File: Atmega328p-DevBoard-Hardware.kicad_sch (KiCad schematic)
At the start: 28 parts, among them J1 Barrel_Jack, J2 DBG/PROG, J3 MTR1-CON, J4 MTR2-CON, SW1 SW_SPST, U1 L7805, U2 ATmega328P-A, U3 L293D, Y1 LFXTAL003237-Crystal-16MHz

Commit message: completed ssd section
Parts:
- added C16: 10uf, Capacitor_SMD:C_0805_2012Metric_Pad1.18x1.45mm_HandSolder, symbol Device:C_Small
- added C17: 0.1uf, Capacitor_SMD:C_0805_2012Metric_Pad1.18x1.45mm_HandSolder, symbol Device:C_Small
- added R10, R11, R12, R13, R14, R15: 1K, Resistor_SMD:R_0805_2012Metric_Pad1.20x1.40mm_HandSolder, symbol Device:R_Small_US
- added R3, R4, R5, R6, R7, R8, R9: 330R, Resistor_SMD:R_0805_2012Metric_Pad1.20x1.40mm_HandSolder, symbol Device:R_Small_US
- added U4: CD4511BE, Package_DIP:DIP-16_W7.62mm_LongPads, symbol 4xxx_IEEE:4511
- added U5: SC39-11YWA, Display_7Segment:Sx39-1xxxxx, symbol Display_Character:SC39-11YWA
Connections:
- net +5V: now also C16.1, C17.1, U4.16 (Vdd)
- net GND: now also C16.2, C17.2, R10.1, R11.1, R12.1, R13.1, R14.1, R15.1, U4.5 (~{EL}), U4.8 (Vss), U5.3 (CC), U5.8 (CC)
- new net: R5.1, U4.11 (Qc)
- new net: R5.2, U5.7 (C)
- new net: R7.1, U4.9 (Qe)
- new net: R7.2, U5.4 (E)
- new net: R3.1, U4.13 (Qa)
- new net: R3.2, U5.10 (A)
- new net: R6.1, U4.10 (Qd)
- new net: R6.2, U5.5 (D)
- new net: R8.1, U4.15 (Qf)
- new net: R8.2, U5.2 (F)
- new net: R4.1, U4.12 (Qb)
- new net: R4.2, U5.9 (B)
- new net: R9.1, U4.14 (Qg)
- new net: R9.2, U5.1 (G)
- new net BLANKING_INPUT_BL: R15.2, U4.4 (~{BI})
- new net LAMP_TEST_LT: R14.2, U4.3 (~{LT})
- new net SSD_A: R10.2, U4.7 (DA)
- new net SSD_B: R11.2, U4.1 (DB)
- new net SSD_C: R12.2, U4.2 (DC)
- new net SSD_D: R13.2, U4.6 (DD)
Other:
- moved on the sheet: C1, C12, C13, C14, C15, C2, C3, C4, D1, D2, J1, J3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

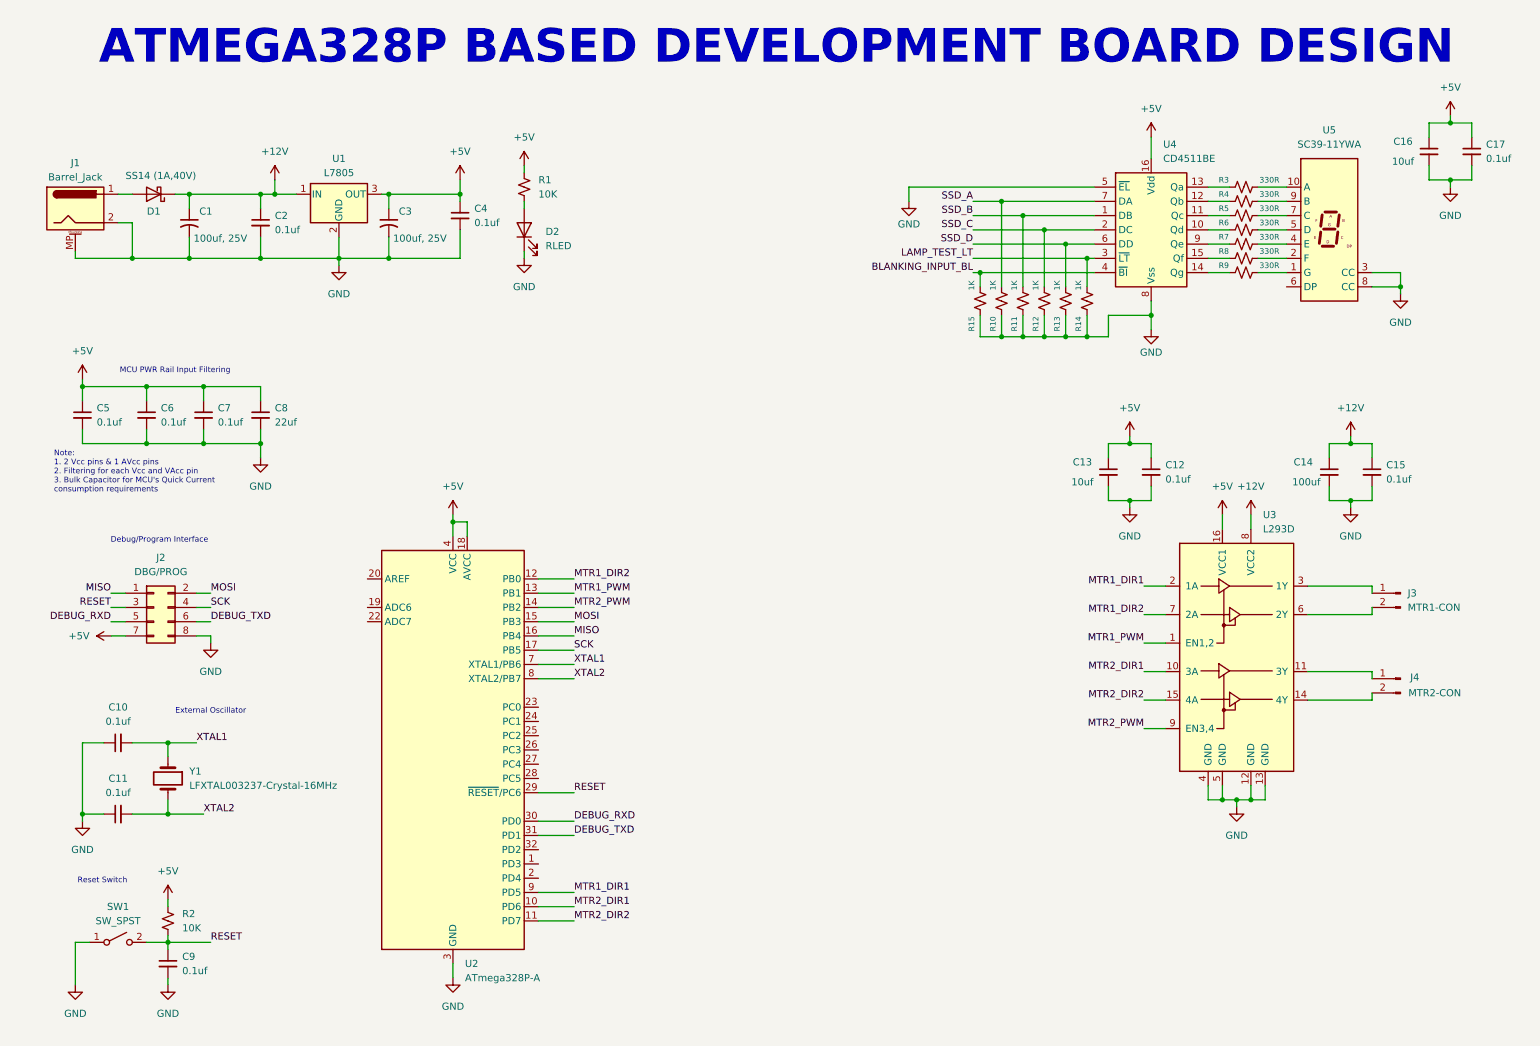
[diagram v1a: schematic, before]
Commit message: finsihed with schematic design, now starting pcb design section
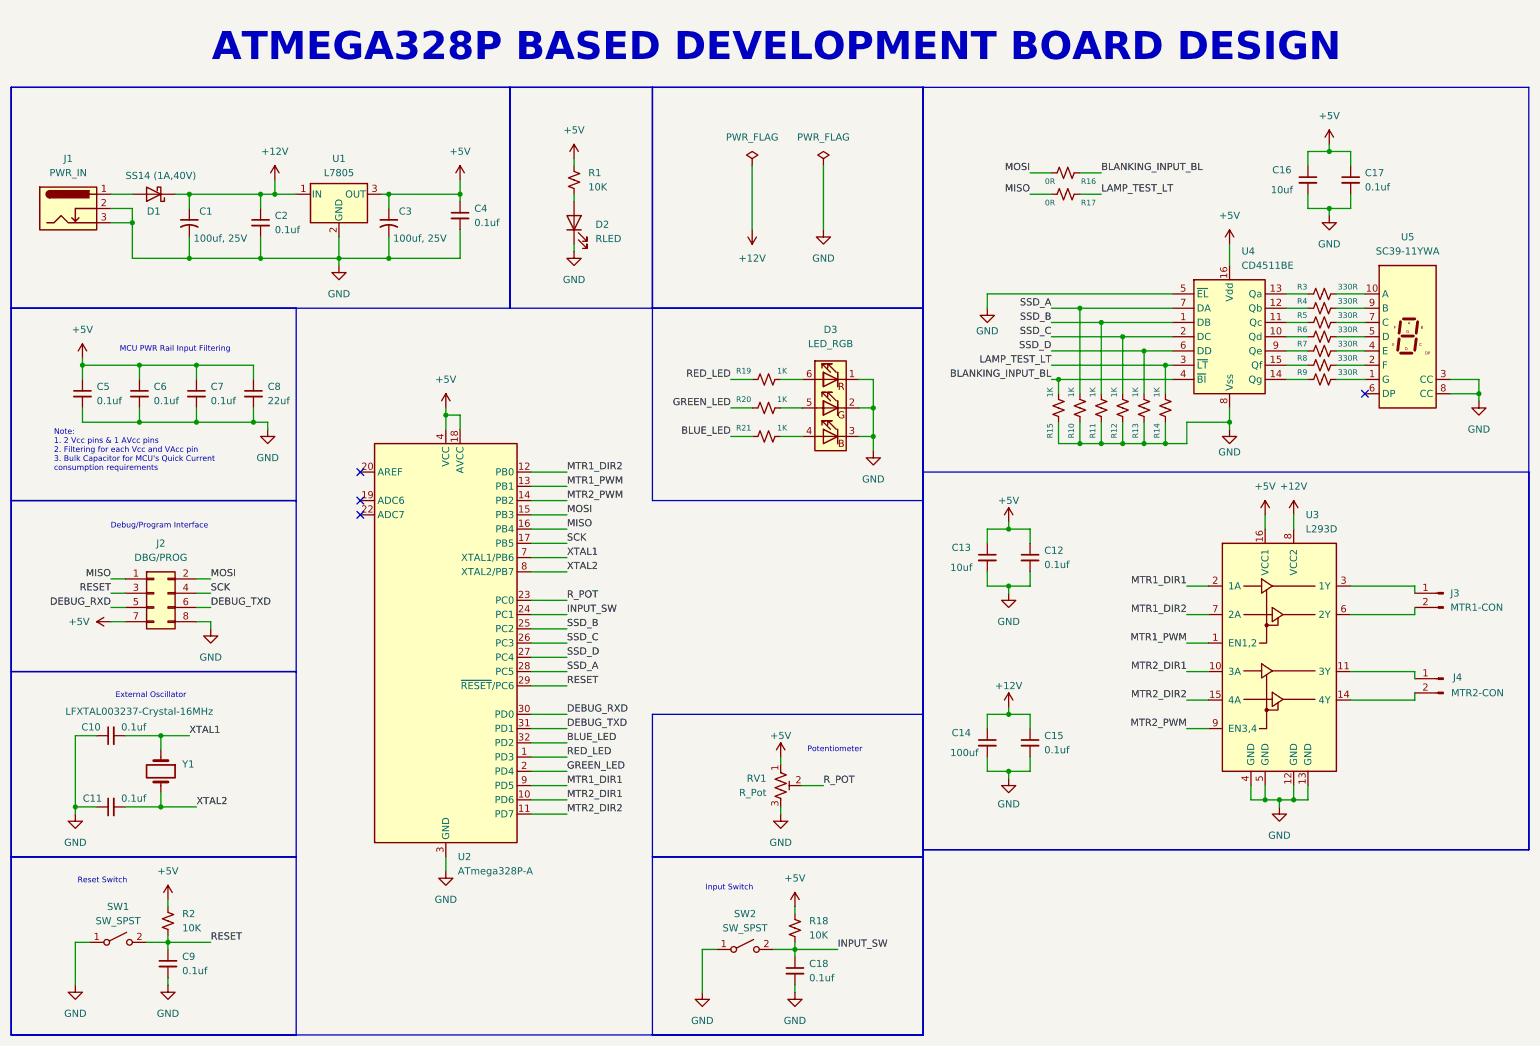
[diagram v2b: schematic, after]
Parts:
- removed J1: Barrel_Jack, Connector_BarrelJack:BarrelJack_Horizontal, symbol Connector:Barrel_Jack_MountingPin
- added C18: 0.1uf, Capacitor_SMD:C_0805_2012Metric_Pad1.18x1.45mm_HandSolder, symbol Device:C_Small
- added D3: LED_RGB, LED_SMD:LED_RGB_5050-6, symbol Device:LED_RGB
- added J1: PWR_IN, Connector_BarrelJack:BarrelJack_Horizontal, symbol Connector:Barrel_Jack_Switch_Pin3Ring
- added R16, R17: 0R, Resistor_SMD:R_0805_2012Metric_Pad1.20x1.40mm_HandSolder, symbol Device:R_Small_US
- added R18: 10K, Resistor_SMD:R_0805_2012Metric_Pad1.20x1.40mm_HandSolder, symbol Device:R_Small_US
- added R19, R20, R21: 1K, Resistor_SMD:R_0805_2012Metric_Pad1.20x1.40mm_HandSolder, symbol Device:R_Small_US
- added RV1: R_Pot, Potentiometer_THT:Potentiometer_Bourns_3386P_Vertical, symbol Device:R_Potentiometer_Trim_US
- added SW2: SW_SPST, Button_Switch_THT:SW_PUSH_6mm, symbol Switch:SW_SPST
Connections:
- net +5V: now also R18.1, RV1.1
- net BLANKING_INPUT_BL: now also R16.1
- net GND: now also C18.2, D3.1 (RK), D3.2 (GK), D3.3 (BK), J1.2, J1.3, RV1.3, SW2.1 (A)
- net LAMP_TEST_LT: now also R17.1
- net MISO: now also R17.2
- net MOSI: now also R16.2
- net SSD_A: now also U2.28 (PC5)
- net SSD_B: now also U2.25 (PC2)
- net SSD_C: now also U2.26 (PC3)
- net SSD_D: now also U2.27 (PC4)
- net at D1.2 (A): now also J1.1
- net RED_LED: now reaches U2.1 (PD3)
- net RED_LED: now also R19.1
- net GREEN_LED: now reaches U2.2 (PD4)
- net GREEN_LED: now also R20.1
- net R_POT: now reaches U2.23 (PC0)
- net R_POT: now also RV1.2
- net INPUT_SW: now reaches U2.24 (PC1)
- net INPUT_SW: now also C18.1, R18.2, SW2.2 (B)
- net BLUE_LED: now reaches U2.32 (PD2)
- net BLUE_LED: now also R21.1
- new net: D3.5 (GA), R20.2
- new net: D3.4 (BA), R21.2
- new net: D3.6 (RA), R19.2
- no-connect marks 0 -> 4
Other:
- note added: "Input Switch"
- note added: "Potentiometer"
- moved on the sheet: C10, C11, C12, C13, C14, C15, C16, C17, C5, C6, C7, C8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

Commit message: Updated schematics wrt footprint selections and mounting holes, and pcb component placement in-progress
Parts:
- added H1, H2, H3, H4: MountingHole, MountingHole:MountingHole_3.2mm_M3_DIN965, symbol Mechanical:MountingHole
- J2: footprint Connector_PinSocket_2.54mm:PinSocket_2x04_P2.54mm_Vertical -> Connector_PinHeader_2.54mm:PinHeader_2x04_P2.54mm_Vertical
- RV1: footprint Potentiometer_THT:Potentiometer_Bourns_3386P_Vertical -> Potentiometer_THT:Potentiometer_Bourns_3296W_Vertical
- SW1, SW2: footprint Button_Switch_THT:SW_PUSH_6mm -> Button_Switch_SMD:SW_Tactile_SPST_NO_Straight_CK_PTS636Sx25SMTRLFS
- Y1: footprint Crystal:Crystal_SMD_HC49-SD_HandSoldering -> Crystal:Crystal_SMD_HC49-SD
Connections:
- net +5V: now also RV1.3; no longer RV1.1
- net GND: now also RV1.1; no longer RV1.3

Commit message: Updated Schematics and Footprints, Finished with Component Placements
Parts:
- removed R16, R17: 0R, Resistor_SMD:R_0805_2012Metric_Pad1.20x1.40mm_HandSolder, symbol Device:R_Small_US
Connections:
- net BLANKING_INPUT_BL: now also U2.19 (ADC6)
- net LAMP_TEST_LT: now also U2.22 (ADC7)
- no-connect marks 4 -> 2
